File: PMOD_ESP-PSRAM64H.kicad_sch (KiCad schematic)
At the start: 4 parts, among them J1 Conn_02x06_Odd_Even, U1 ESP-PSRAM64H

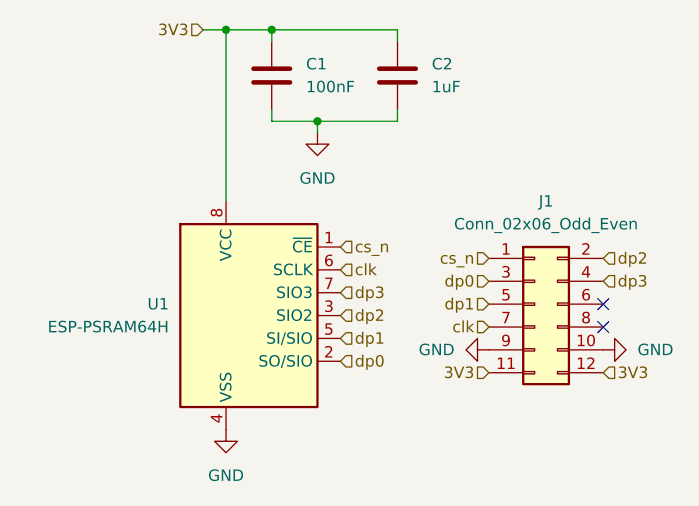
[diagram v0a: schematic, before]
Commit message: fix: swap dp0, dp1 pins
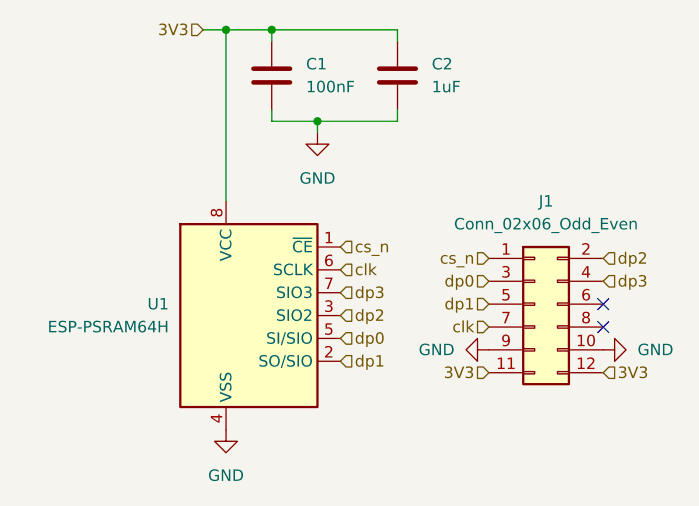
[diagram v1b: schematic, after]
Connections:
- net dp0: now also U1.5 (SI/SIO); no longer U1.2 (SO/SIO)
- net dp1: now also U1.2 (SO/SIO); no longer U1.5 (SI/SIO)
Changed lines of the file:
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@@
+		)
+	)
+	(hierarchical_label "dp1"
+		(shape input)
+		(at 158.75 93.98 0)
+		(fields_autoplaced yes)
+		(effects
+			(font
+				(size 1.27 1.27)
+			)
+			(justify left)
+		)
+	)
+	(hierarchical_label "dp0"
+		(shape input)
+		(at 158.75 91.44 0)
+		(fields_autoplaced yes)
+		(effects
+			(font
+				(size 1.27 1.27)
+			)
+			(justify left)
 		)
 	)
@@
 		)
 	)
-	(hierarchical_label "dp1"
-		(shape input)
-		(at 158.75 91.44 0)
-		(fields_autoplaced yes)
-		(effects
-			(font
-				(size 1.27 1.27)
-			)
-			(justify left)
-		)
-	)
 	(hierarchical_label "3V3"
 		(shape input)
@@
 		(fields_autoplaced yes)
 		(effects
-			(font
-				(size 1.27 1.27)
-			)
-			(justify left)
-		)
-	)
-	(hierarchical_label "dp0"
-		(shape input)
-		(at 158.75 93.98 0)
-		(fields_autoplaced yes)
-		(effects
